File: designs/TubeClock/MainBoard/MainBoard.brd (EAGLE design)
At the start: 98 x 67 mm, 45 parts, among them IC1 LD117ADT-TR, J1 S2B-NSHSS-TB, J2 S2B-NSHSS-TB, J3 S2B-NSHSS-TB, J4 PJ-002AH-SMT-TR, J5 S2B-NSHSS-TB, Q1 2N7002NXAKR, Q2 2N7002NXAKR

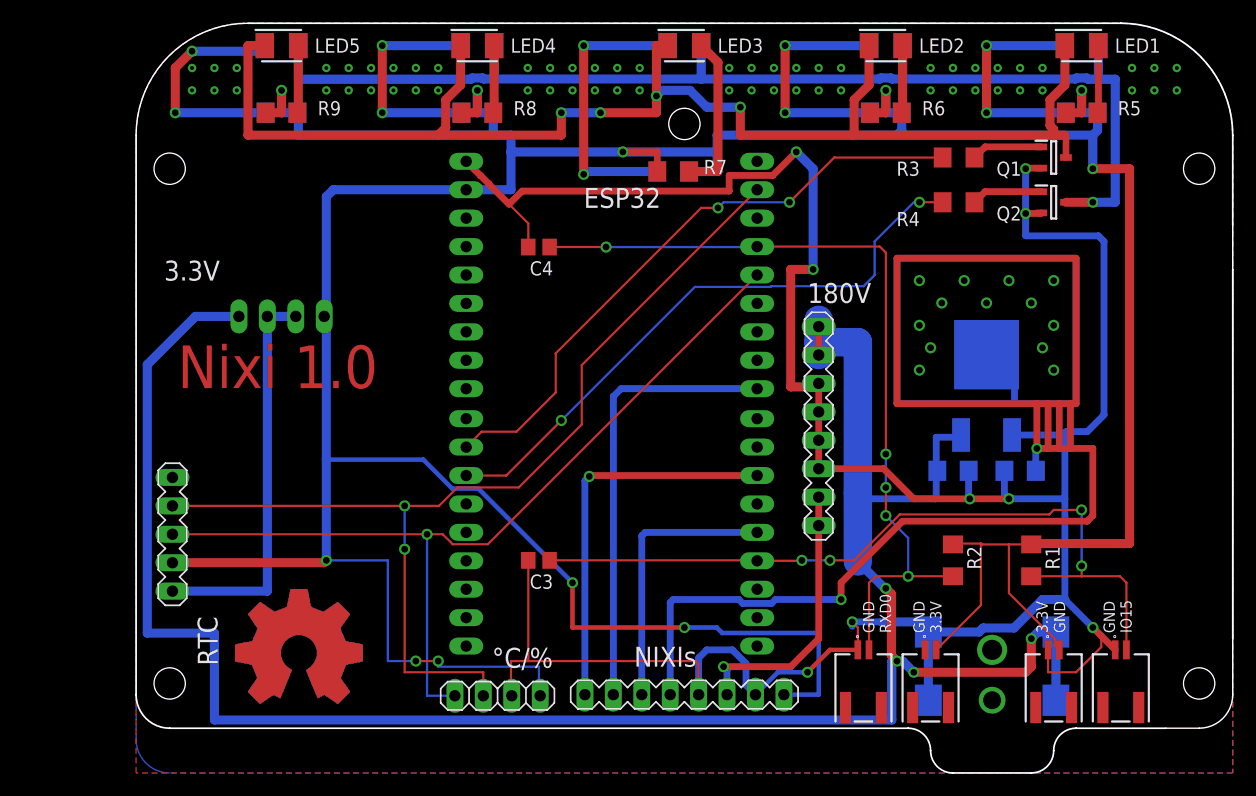
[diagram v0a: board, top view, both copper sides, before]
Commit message: changed mainboard design radio
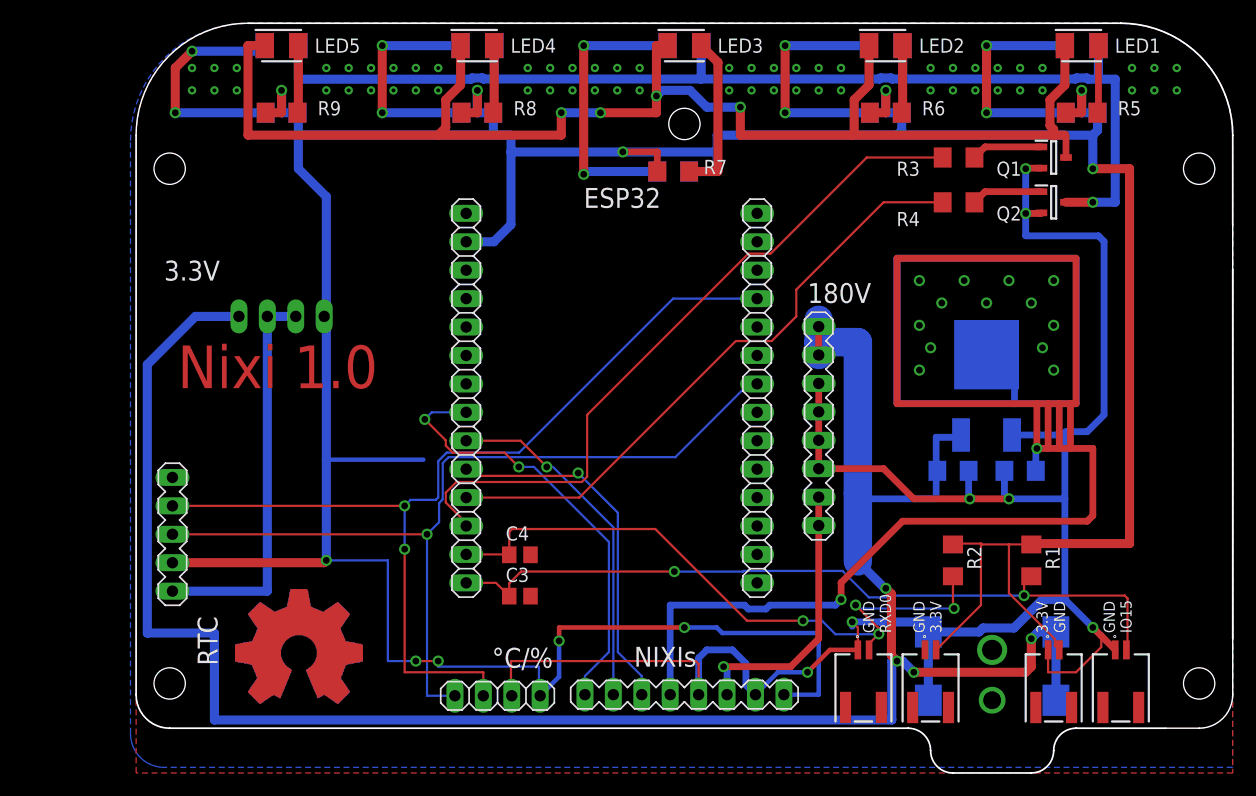
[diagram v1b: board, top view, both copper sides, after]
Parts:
- removed SV2, SV3, SV4, SV5: (no value), CommonParts:MA09-1
- added JP3, JP4: (no value), pinhead:1X14
- moved C4 27.6 mm to (34.3, 15.5), turned to 0 degrees
- moved C3 3.62 mm to (34.3, 11.8), turned to 0 degrees
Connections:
- removed net CLK: SV4.9
- removed net CMD: SV3.1
- removed net EN: SV2.7
- removed net GPIO12: SV3.5
- removed net GPIO13: SV3.4
- removed net GPIO14: SV3.6
- removed net IO0: SV4.4
- removed net IO15: C3.1, J1.2, R1.2, SV4.6
- removed net IO18: SV5.8
- removed net IO19: SV5.7
- removed net IO2: SV1.3, SV4.5
- removed net IO23: SV5.1
- removed net IO4: SV1.1, SV4.3
- removed net IO5: SV1.2, SV5.9
- removed net NC_1: SV4.2
- removed net NC_2: SV4.1
- removed net NC_3: SV5.6
- removed net SD0: SV4.8
- removed net SD1: SV4.7
- removed net SD2: SV3.3
- removed net SD3: SV3.2
- removed net SEN_VN: SV2.5
- removed net SEN_VP: SV2.6
- new net IO12: C4.1, J3.2, JP3.13, R2.2
- new net IO13: C3.1, J1.2, JP3.14, R1.2
- new net IO14: JP3.12, R3.1
- new net SENSOR_VN: JP3.4
- new net SENSOR_VP: JP3.3
- net 3.3V: now also JP3.2; no longer SV2.8
- net GND: now also JP3.1, JP4.12, JP4.13, JP4.14; no longer SV2.9
- net IO21: now also JP4.8; no longer SV5.5
- net IO22: now also JP4.11; no longer SV5.2
- net IO25: now also JP3.9, SV1.2; no longer SV3.9
- net IO26: now also JP3.10, SV1.3; no longer R3.1, SV3.8
- net IO27: now also JP3.11; no longer SV3.7
- net IO32: now also JP3.7; no longer SV2.2
- net IO33: now also JP3.8, SV1.1; no longer SV2.1
- net IO34: now also JP3.5; no longer SV2.4
- net IO35: now also JP3.6; no longer SV2.3
- net RXD0: now also JP4.9; no longer C4.1, J3.2, R2.2, SV5.4
- net TXD0: now also JP4.10; no longer SV5.3
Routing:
- net GND: track 296.2 -> 217.2 mm, vias 9 -> 7
- net RXD0: track 73.9 -> 0.00 mm, vias 5 -> 0
- net IO15: track 70.6 -> 0.00 mm, vias 4 -> 0
- net IO13: track 0.00 -> 69.0 mm, vias 0 -> 2
- net IO14: track 0.00 -> 63.8 mm
- net IO12: track 0.00 -> 60.0 mm, vias 0 -> 4
- net IO5: track 39.8 -> 0.00 mm
- net IO33: track 0.00 -> 39.8 mm, vias 0 -> 2
- net IO4: track 34.7 -> 0.00 mm, vias 1 -> 0
- net IO25: track 0.00 -> 31.3 mm, vias 0 -> 1
- net IO2: track 24.6 -> 0.00 mm
- net IO26: track 55.3 -> 32.5 mm, vias 2 -> 1
- net 3.3V: track 356.3 -> 339.9 mm
- net IO22: track 91.2 -> 86.0 mm
- net IO21: track 79.7 -> 77.8 mm
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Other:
- board text removed: "CLK"
- board text removed: "GPIO12"
- board text removed: "GPIO13"
- board text removed: "GPIO14"
- board text removed: "IO0"
- board text removed: "IO18"
- board text removed: "IO19"
- board text removed: "IO2"
- board text removed: "IO21"
- board text removed: "IO22"
- board text removed: "IO23"
- board text removed: "IO25"
- board text removed: "IO26"
- board text removed: "IO27"
- board text removed: "IO32"
- board text removed: "IO33"
- board text removed: "IO34"
- board text removed: "IO35"
- board text removed: "IO4"
- board text removed: "IO5"
- board text removed: "NC_1"
- board text removed: "NC_2"
- board text removed: "NC_3"
- board text removed: "SD0"
- board text removed: "SD1"
- board text removed: "SD2"
- board text removed: "SD3"
- board text removed: "SEN_VN"
- board text removed: "SEN_VP"
- board text removed: "TXD0"
